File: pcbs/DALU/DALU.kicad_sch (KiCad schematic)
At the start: 1 part, among them J101 Conn_02x20_Odd_Even

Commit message: Last of the compute stages
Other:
- added sheet OR (OR.kicad_sch)
- sheet XOR ports: added A_{bus}, B_{bus}, XOR_{bus}; removed none
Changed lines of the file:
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@@
   (junction (at 46.99 68.58) (diameter 0) (color 0 0 0 0)
   )
+  (junction (at 82.55 46.99) (diameter 0) (color 0 0 0 0)
+  )
   (junction (at 78.74 29.21) (diameter 0) (color 0 0 0 0)
   )
   (junction (at 25.4 68.58) (diameter 0) (color 0 0 0 0)
   )
+  (junction (at 78.74 72.39) (diameter 0) (color 0 0 0 0)
+  )
+  (junction (at 78.74 52.07) (diameter 0) (color 0 0 0 0)
+  )
+  (junction (at 82.55 67.31) (diameter 0) (color 0 0 0 0)
+  )
   (bus_entry (at 60.96 50.8) (size -2.54 2.54)
     (stroke (width 0) (type default) (color 0 0 0 0))
@@
     (stroke (width 0) (type default) (color 0 0 0 0))
   )
+  (bus (pts (xy 78.74 52.07) (xy 78.74 72.39))
+    (stroke (width 0) (type default) (color 0 0 0 0))
+  )
   (bus (pts (xy 58.42 38.1) (xy 58.42 40.64))
     (stroke (width 0) (type default) (color 0 0 0 0))
@@
     (stroke (width 0) (type default) (color 0 0 0 0))
   )
+  (bus (pts (xy 78.74 72.39) (xy 87.63 72.39))
+    (stroke (width 0) (type default) (color 0 0 0 0))
+  )
   (wire (pts (xy 16.51 68.58) (xy 25.4 68.58))
     (stroke (width 0) (type default) (color 0 0 0 0))
@@
     (stroke (width 0) (type default) (color 0 0 0 0))
   )
+  (bus (pts (xy 78.74 72.39) (xy 78.74 91.44))
+    (stroke (width 0) (type default) (color 0 0 0 0))
+  )
+  (bus (pts (xy 82.55 67.31) (xy 87.63 67.31))
+    (stroke (width 0) (type default) (color 0 0 0 0))
+  )
+  (bus (pts (xy 82.55 46.99) (xy 82.55 67.31))
+    (stroke (width 0) (type default) (color 0 0 0 0))
+  )
   (wire (pts (xy 43.18 33.02) (xy 55.88 33.02))
     (stroke (width 0) (type default) (color 0 0 0 0))
@@
     (stroke (width 0) (type default) (color 0 0 0 0))
   )
+  (bus (pts (xy 82.55 67.31) (xy 82.55 87.63))
+    (stroke (width 0) (type default) (color 0 0 0 0))
+  )
   (wire (pts (xy 43.18 63.5) (xy 58.42 63.5))
     (stroke (width 0) (type default) (color 0 0 0 0))
@@
     (stroke (width 0) (type default) (color 0 0 0 0))
   )
+  (bus (pts (xy 78.74 91.44) (xy 87.63 91.44))
+    (stroke (width 0) (type default) (color 0 0 0 0))
+  )
   (bus (pts (xy 58.42 35.56) (xy 58.42 38.1))
     (stroke (width 0) (type default) (color 0 0 0 0))
@@
   )
   (wire (pts (xy 43.18 35.56) (xy 55.88 35.56))
+    (stroke (width 0) (type default) (color 0 0 0 0))
+  )
+  (bus (pts (xy 82.55 87.63) (xy 87.63 87.63))
     (stroke (width 0) (type default) (color 0 0 0 0))
   )
@@
       (effects (font (size 1.27 1.27)) (justify left top))
     )
+    (pin "A_{bus}" input (at 87.63 67.31 180)
+      (effects (font (size 1.27 1.27)) (justify left))
+    )
+    (pin "B_{bus}" input (at 87.63 72.39 180)
+      (effects (font (size 1.27 1.27)) (justify left))
+    )
+    (pin "XOR_{bus}" output (at 106.68 69.85 0)
+      (effects (font (size 1.27 1.27)) (justify right))
+    )
   )
   (sheet (at 87.63 22.86) (size 19.05 13.97) (fields_autoplaced)
@@
     )
   )
+  (sheet (at 87.63 83.82) (size 19.05 11.43) (fields_autoplaced)
+    (stroke (width 0.1524) (type solid) (color 0 0 0 0))
+    (fill (color 0 0 0 0.0000))
+    (property "Sheet name" "OR" (id 0) (at 87.63 83.1084 0)
+      (effects (font (size 1.27 1.27)) (justify left bottom))
+    )
+    (property "Sheet file" "OR.kicad_sch" (id 1) (at 87.63 95.8346 0)
+      (effects (font (size 1.27 1.27)) (justify left top))
+    )
+    (pin "A_{bus}" input (at 87.63 87.63 180)
+      (effects (font (size 1.27 1.27)) (justify left))
+    )
+    (pin "B_{bus}" input (at 87.63 91.44 180)
+      (effects (font (size 1.27 1.27)) (justify left))
+    )
+    (pin "OR_{bus}" output (at 106.68 88.9 0)
+      (effects (font (size 1.27 1.27)) (justify right))
+    )
+  )
   (sheet (at 87.63 43.18) (size 19.05 13.97) (fields_autoplaced)
     (stroke (width 0.1524) (type solid) (color 0 0 0 0))
@@
     (path "/c6ea6b53-9211-4c3c-9fbd-19ff7075ec1c" (page "3"))
     (path "/12f01842-90c1-4b07-bb63-297dee23d62f" (page "4"))
+    (path "/95c8ed90-5067-42ef-af82-1a4d464a971b" (page "5"))
   )
   (symbol_instances
@@
       (reference "#PWR0201") (unit 1) (value "GND") (footprint "")
     )
+    (path "/95c8ed90-5067-42ef-af82-1a4d464a971b/d2917962-5a4a-4a69-aaf2-f43483f15313"
+      (reference "#PWR?") (unit 1) (value "GND") (footprint "")
+    )
+    (path "/95c8ed90-5067-42ef-af82-1a4d464a971b/4a3697d2-7faa-484a-8bcb-b8e25fa6ff72"
+      (reference "D501") (unit 1) (value "1N4148") (footprint "Diode_THT:D_DO-35_SOD27_P7.62mm_Horizontal")
+    )
+    (path "/95c8ed90-5067-42ef-af82-1a4d464a971b/bb7d2965-ee1e-4dec-a199-3e00f2e0bc28"
+      (reference "D502") (unit 1) (value "1N4148") (footprint "Diode_THT:D_DO-35_SOD27_P7.62mm_Horizontal")
+    )
+    (path "/95c8ed90-5067-42ef-af82-1a4d464a971b/a1a7e2eb-7c7a-416d-b49a-5a4e31e405d0"
+      (reference "D503") (unit 1) (value "1N4148") (footprint "Diode_THT:D_DO-35_SOD27_P7.62mm_Horizontal")
+    )
+    (path "/95c8ed90-5067-42ef-af82-1a4d464a971b/e2dd1ad3-44c2-4bb1-b77e-ec4191e188b1"
+      (reference "D504") (unit 1) (value "1N4148") (footprint "Diode_THT:D_DO-35_SOD27_P7.62mm_Horizontal")
+    )
+    (path "/95c8ed90-5067-42ef-af82-1a4d464a971b/07a04b4b-943e-4706-905e-cecf4428214b"
+      (reference "D505") (unit 1) (value "1N4148") (footprint "Diode_THT:D_DO-35_SOD27_P7.62mm_Horizontal")
+    )
+    (path "/95c8ed90-5067-42ef-af82-1a4d464a971b/af0b345b-54e7-42a3-a286-538b1287836d"
+      (reference "D506") (unit 1) (value "1N4148") (footprint "Diode_THT:D_DO-35_SOD27_P7.62mm_Horizontal")
+    )
+    (path "/95c8ed90-5067-42ef-af82-1a4d464a971b/421d6b09-7fac-4770-86f8-5100d23c67b1"
+      (reference "D507") (unit 1) (value "1N4148") (footprint "Diode_THT:D_DO-35_SOD27_P7.62mm_Horizontal")
+    )
+    (path "/95c8ed90-5067-42ef-af82-1a4d464a971b/569a1e0a-7613-401f-98cd-f7d7ae658bd9"
+      (reference "D508") (unit 1) (value "1N4148") (footprint "Diode_THT:D_DO-35_SOD27_P7.62mm_Horizontal")
+    )
+    (path "/95c8ed90-5067-42ef-af82-1a4d464a971b/98e6afcd-7c0c-46fa-aa45-ceb39f9dcfaf"
+      (reference "D509") (unit 1) (value "1N4148") (footprint "Diode_THT:D_DO-35_SOD27_P7.62mm_Horizontal")
+    )
+    (path "/95c8ed90-5067-42ef-af82-1a4d464a971b/60bbdc9b-d936-4faf-9e28-6b40f0fd6cbf"
+      (reference "D510") (unit 1) (value "1N4148") (footprint "Diode_THT:D_DO-35_SOD27_P7.62mm_Horizontal")
+    )
+    (path "/95c8ed90-5067-42ef-af82-1a4d464a971b/fada2b91-ce17-4b8b-b1c7-d90cada8f840"
+      (reference "D511") (unit 1) (value "1N4148") (footprint "Diode_THT:D_DO-35_SOD27_P7.62mm_Horizontal")
+    )
+    (path "/95c8ed90-5067-42ef-af82-1a4d464a971b/1894f8d6-098f-4396-911d-8aaa729e1f4d"
+      (reference "D512") (unit 1) (value "1N4148") (footprint "Diode_THT:D_DO-35_SOD27_P7.62mm_Horizontal")
+    )
+    (path "/95c8ed90-5067-42ef-af82-1a4d464a971b/29edd219-0759-4f76-a9cf-bbf5f6d146f1"
+      (reference "D513") (unit 1) (value "1N4148") (footprint "Diode_THT:D_DO-35_SOD27_P7.62mm_Horizontal")
+    )
+    (path "/95c8ed90-5067-42ef-af82-1a4d464a971b/05c0b09a-3745-46e5-8419-974dbbc659de"
+      (reference "D514") (unit 1) (value "1N4148") (footprint "Diode_THT:D_DO-35_SOD27_P7.62mm_Horizontal")
+    )
+    (path "/95c8ed90-5067-42ef-af82-1a4d464a971b/958ba730-cb10-4605-bd9f-9622ef54c965"
+      (reference "D515") (unit 1) (value "1N4148") (footprint "Diode_THT:D_DO-35_SOD27_P7.62mm_Horizontal")
+    )
+    (path "/95c8ed90-5067-42ef-af82-1a4d464a971b/2b0a17ac-d926-4d0e-b18e-f9a3a2894ef9"
+      (reference "D516") (unit 1) (value "1N4148") (footprint "Diode_THT:D_DO-35_SOD27_P7.62mm_Horizontal")
+    )
     (path "/0078be7f-ebde-4855-a007-c3409b021a3e"
       (reference "J101") (unit 1) (value "Conn_02x20_Odd_Even") (footprint "Connector_PinHeader_2.54mm:PinHeader_2x20_P2.54mm_Vertical")
     )
+    (path "/95c8ed90-5067-42ef-af82-1a4d464a971b/9b8f5155-1304-4993-8373-bc373de0a39a"
+      (reference "R501") (unit 1) (value "100k") (footprint "Resistor_THT:R_Axial_DIN0207_L6.3mm_D2.5mm_P7.62mm_Horizontal")
+    )
+    (path "/95c8ed90-5067-42ef-af82-1a4d464a971b/158d25e5-8ec9-4037-a0c2-61fe1e6ce44b"
+      (reference "R502") (unit 1) (value "100k") (footprint "Resistor_THT:R_Axial_DIN0207_L6.3mm_D2.5mm_P7.62mm_Horizontal")
+    )
+    (path "/95c8ed90-5067-42ef-af82-1a4d464a971b/f4092d13-ae6a-4ea0-837d-8731ed399cc1"
+      (reference "R503") (unit 1) (value "100k") (footprint "Resistor_THT:R_Axial_DIN0207_L6.3mm_D2.5mm_P7.62mm_Horizontal")
+    )
+    (path "/95c8ed90-5067-42ef-af82-1a4d464a971b/872041c3-3b2a-4e80-9cc8-3a2c263148c4"
+      (reference "R504") (unit 1) (value "100k") (footprint "Resistor_THT:R_Axial_DIN0207_L6.3mm_D2.5mm_P7.62mm_Horizontal")
+    )
+    (path "/95c8ed90-5067-42ef-af82-1a4d464a971b/d5f1b087-ebb8-409e-b54e-e6f86f6d7838"
+      (reference "R505") (unit 1) (value "100k") (footprint "Resistor_THT:R_Axial_DIN0207_L6.3mm_D2.5mm_P7.62mm_Horizontal")
+    )
+    (path "/95c8ed90-5067-42ef-af82-1a4d464a971b/aeb0dafe-31b3-4371-a164-439c8eb5842e"
+      (reference "R506") (unit 1) (value "100k") (footprint "Resistor_THT:R_Axial_DIN0207_L6.3mm_D2.5mm_P7.62mm_Horizontal")
+    )
+    (path "/95c8ed90-5067-42ef-af82-1a4d464a971b/563e37ab-bd17-438f-98ec-d1d2cc39a8d4"
+      (reference "R507") (unit 1) (value "100k") (footprint "Resistor_THT:R_Axial_DIN0207_L6.3mm_D2.5mm_P7.62mm_Horizontal")
+    )
+    (path "/95c8ed90-5067-42ef-af82-1a4d464a971b/95fb95c2-98e6-41b7-ac87-417ac8aebac9"
+      (reference "R508") (unit 1) (value "100k") (footprint "Resistor_THT:R_Axial_DIN0207_L6.3mm_D2.5mm_P7.62mm_Horizontal")
+    )
     (path "/70795f93-2efa-413c-baa8-a557a86ea734/e43fe007-808a-4034-8733-705344372de1"

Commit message: Trying to figure out the hierarchical buses
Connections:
- net C0: now reaches J101.3 (Pin_3)
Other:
- added sheet Output Stage (output.kicad_sch)
- sheet AND-NAND ports: added A[0..7], B[0..7], NAND[0..7]; removed AND/NAND_{bus}, A_{bus}, B_{bus}
- sheet Adder-Subtractor ports: added AS[0..7], A[0..7], B[0..7]; removed ADD/SUB_{bus}, A_{bus}, B_{bus}
- sheet OR ports: added A[0..7], B[0..7], OR[0..7]; removed A_{bus}, B_{bus}, OR_{bus}
- sheet XOR ports: added A[0..7], B[0..7], XOR[0..7]; removed A_{bus}, B_{bus}, XOR_{bus}

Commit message: Trying to get everything together
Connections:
- net A0: no longer names the net of J101.18 (Pin_18)
- net A1: no longer names the net of J101.16 (Pin_16)
- net A2: no longer names the net of J101.14 (Pin_14)
- net A3: no longer names the net of J101.12 (Pin_12)
- net A4: no longer names the net of J101.10 (Pin_10)
- net A5: no longer names the net of J101.8 (Pin_8)
- net A6: no longer names the net of J101.6 (Pin_6)
- net A7 renamed A.A7
- net C0 renamed C_{bus}0
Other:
- sheet Adder-Subtractor renamed AdderSubtractor
- sheet Output Stage ports: added ADDSUB[0..7], C_{bus}[0..7]; removed AS[0..7], C_{bus}

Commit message: Thinking about some of the control logic
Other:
- sheet Output Stage ports: added none; removed C_{bus}[0..7]

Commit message: Thinking about SMD assembly. Will be rethinking
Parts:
- added U101, U102: 74HC245, Package_SO:SOIC-20W_7.5x12.8mm_P1.27mm, symbol 74xx:74HC245
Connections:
- net at J101.10 (Pin_10): now also U101.5 (A3)
- net at J101.12 (Pin_12): now also U101.6 (A4)
- net at J101.14 (Pin_14): now also U101.7 (A5)
- net at J101.16 (Pin_16): now also U101.8 (A6)
- net at J101.18 (Pin_18): now also U101.9 (A7)
- net at J101.6 (Pin_6): now also U101.3 (A1)
- net at J101.8 (Pin_8): now also U101.4 (A2)
- net A.A7: no longer names the net of J101.4 (Pin_4)
- net A.A7: now also U101.2 (A0)
- net B0: no longer names the net of J101.38 (Pin_38)
- net B0: now also U102.9 (A7)
- net B1: no longer names the net of J101.36 (Pin_36)
- net B1: now also U102.8 (A6)
- net B2: no longer names the net of J101.34 (Pin_34)
- net B2: now also U102.7 (A5)
- net B3: no longer names the net of J101.32 (Pin_32)
- net B3: now also U102.6 (A4)
- net B4: no longer names the net of J101.30 (Pin_30)
- net B4: now also U102.5 (A3)
- net B5: no longer names the net of J101.28 (Pin_28)
- net B5: now also U102.4 (A2)
- net B6: no longer names the net of J101.26 (Pin_26)
- net B6: now also U102.3 (A1)
- net B7: no longer names the net of J101.24 (Pin_24)
- net B7: now also U102.2 (A0)
- net C_{bus}0: no longer names the net of J101.3 (Pin_3)
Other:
- moved on the sheet: J101

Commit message: Doing some rethinking
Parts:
- removed J101: Conn_02x20_Odd_Even, Connector_PinHeader_2.54mm:PinHeader_2x20_P2.54mm_Vertical, symbol Connector_Generic:Conn_02x20_Odd_Even
- removed U101, U102: 74HC245, Package_SO:SOIC-20W_7.5x12.8mm_P1.27mm, symbol 74xx:74HC245
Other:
- added sheet Connector (connector.kicad_sch)

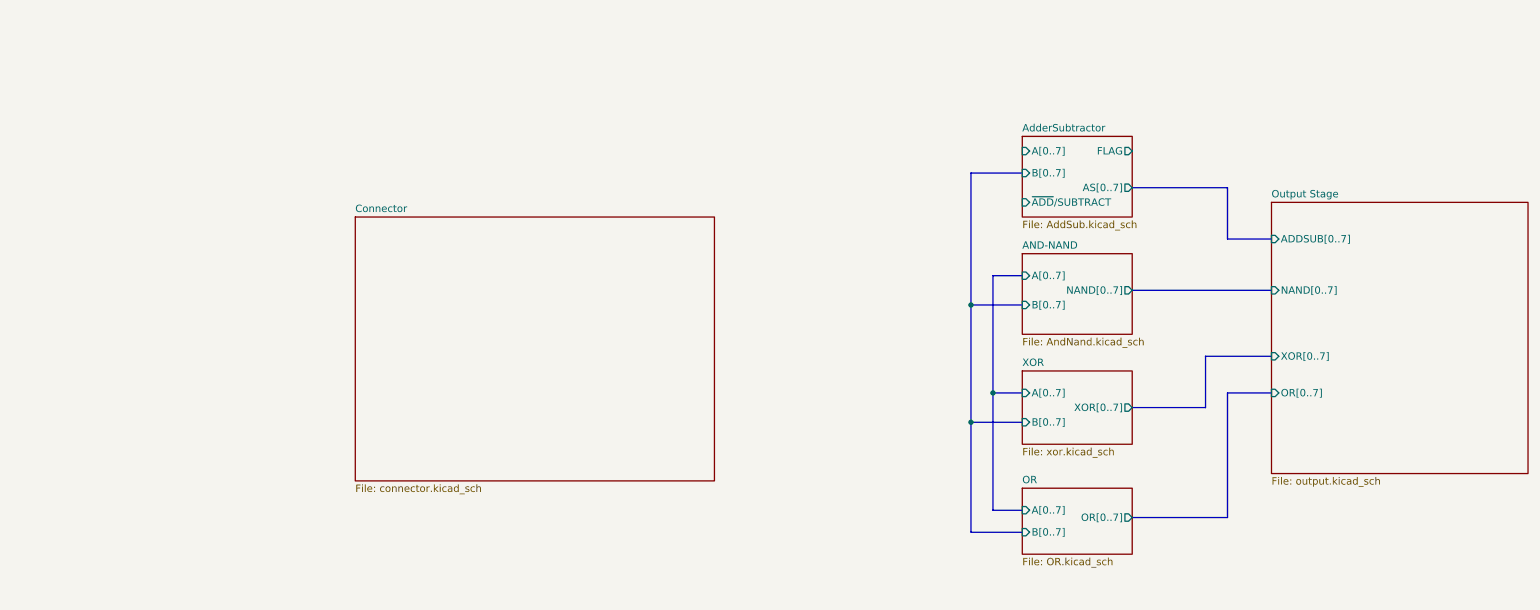
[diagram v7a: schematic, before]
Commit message: Input stage fiddling
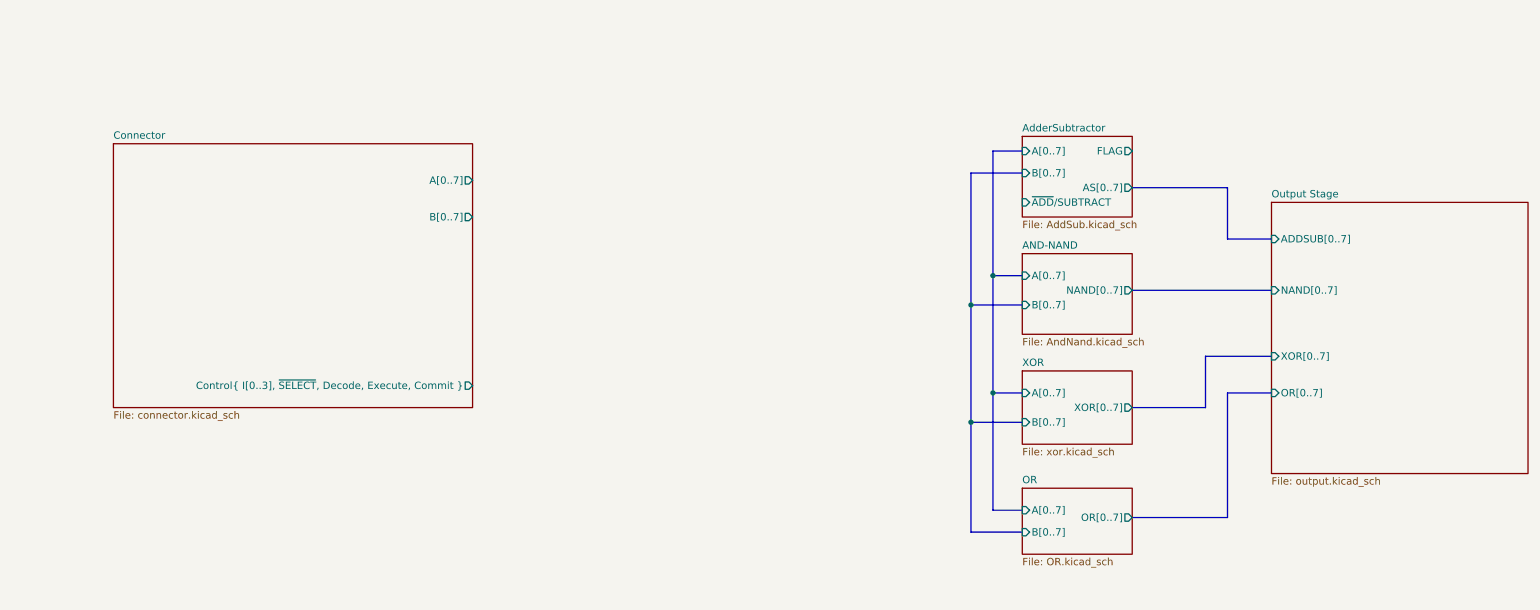
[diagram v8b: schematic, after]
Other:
- sheet Connector ports: added A[0..7], B[0..7], Control{ I[0..3], ~{SELECT}, Decode, Execute, Commit }; removed none
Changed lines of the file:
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@@
   (junction (at 180.34 82.55) (diameter 0) (color 0 0 0 0)
   )
+  (junction (at 184.15 57.15) (diameter 0) (color 0 0 0 0)
+  )
   (junction (at 180.34 62.23) (diameter 0) (color 0 0 0 0)
   )
@@
     (stroke (width 0) (type default) (color 0 0 0 0))
   )
+  (bus (pts (xy 184.15 35.56) (xy 189.23 35.56))
+    (stroke (width 0) (type default) (color 0 0 0 0))
+  )
   (bus (pts (xy 224.79 77.47) (xy 232.41 77.47))
     (stroke (width 0) (type default) (color 0 0 0 0))
@@
   )
   (bus (pts (xy 184.15 57.15) (xy 189.23 57.15))
+    (stroke (width 0) (type default) (color 0 0 0 0))
+  )
+  (bus (pts (xy 184.15 57.15) (xy 184.15 35.56))
     (stroke (width 0) (type default) (color 0 0 0 0))
   )
@@
     )
   )
-  (sheet (at 73.66 46.99) (size 62.23 45.72) (fields_autoplaced)
+  (sheet (at 31.75 34.29) (size 62.23 45.72) (fields_autoplaced)
     (stroke (width 0.1524) (type solid) (color 0 0 0 0))
     (fill (color 0 0 0 0.0000))
-    (property "Sheet name" "Connector" (id 0) (at 73.66 46.2784 0)
+    (property "Sheet name" "Connector" (id 0) (at 31.75 33.5784 0)
       (effects (font (size 1.27 1.27)) (justify left bottom))
     )
-    (property "Sheet file" "connector.kicad_sch" (id 1) (at 73.66 93.2946 0)
+    (property "Sheet file" "connector.kicad_sch" (id 1) (at 31.75 80.5946 0)
       (effects (font (size 1.27 1.27)) (justify left top))
+    )
+    (pin "A[0..7]" output (at 93.98 40.64 0)
+      (effects (font (size 1.27 1.27)) (justify right))
+    )
+    (pin "Control{ I[0..3], ~{SELECT}, Decode, Execute, Commit }" output (at 93.98 76.2 0)
+      (effects (font (size 1.27 1.27)) (justify right))
+    )
+    (pin "B[0..7]" output (at 93.98 46.99 0)
+      (effects (font (size 1.27 1.27)) (justify right))
     )
   )
@@
       (reference "#PWR0718") (unit 1) (value "GND") (footprint "")
     )
+    (path "/5a7cb513-9739-4d2d-a582-8607360c12f9/21d95115-dbd9-470e-8e19-1960bb6f6324"
+      (reference "#PWR?") (unit 1) (value "GND") (footprint "")
+    )
+    (path "/5a7cb513-9739-4d2d-a582-8607360c12f9/80b492a5-fd4d-44b4-9dea-06998740736c"
+      (reference "#PWR?") (unit 1) (value "GND") (footprint "")
+    )
+    (path "/5a7cb513-9739-4d2d-a582-8607360c12f9/d1aa965e-169e-4b67-aca0-50fad862f64e"
+      (reference "#PWR?") (unit 1) (value "GND") (footprint "")
+    )
     (path "/95c8ed90-5067-42ef-af82-1a4d464a971b/4a3697d2-7faa-484a-8bcb-b8e25fa6ff72"
       (reference "D601") (unit 1) (value "1N4148") (footprint "Diode_THT:D_DO-35_SOD27_P7.62mm_Horizontal")
@@
       (reference "U402") (unit 5) (value "74HC00") (footprint "Package_DIP:DIP-14_W7.62mm_Socket")
     )
+    (path "/c6ea6b53-9211-4c3c-9fbd-19ff7075ec1c/0ec7035b-ccb5-43bc-b8f5-bca38c208175"
+      (reference "U403") (unit 1) (value "74HC14") (footprint "Package_SO:SOIC-14_3.9x8.7mm_P1.27mm")
+    )
+    (path "/c6ea6b53-9211-4c3c-9fbd-19ff7075ec1c/292da1ac-5d5b-4b90-a98b-0a23ed154e2a"
+      (reference "U403") (unit 2) (value "74HC14") (footprint "Package_SO:SOIC-14_3.9x8.7mm_P1.27mm")
+    )
+    (path "/c6ea6b53-9211-4c3c-9fbd-19ff7075ec1c/9474edcf-0a86-480e-a097-6025e2d77e58"
+      (reference "U403") (unit 3) (value "74HC14") (footprint "Package_SO:SOIC-14_3.9x8.7mm_P1.27mm")
+    )
+    (path "/c6ea6b53-9211-4c3c-9fbd-19ff7075ec1c/b7cf4de2-e018-4c3e-8ca5-4623af79397a"
+      (reference "U403") (unit 4) (value "74HC14") (footprint "Package_SO:SOIC-14_3.9x8.7mm_P1.27mm")
+    )
+    (path "/c6ea6b53-9211-4c3c-9fbd-19ff7075ec1c/9c79a204-b128-431d-8332-383be6aa4922"
+      (reference "U403") (unit 5) (value "74HC14") (footprint "Package_SO:SOIC-14_3.9x8.7mm_P1.27mm")
+    )
+    (path "/c6ea6b53-9211-4c3c-9fbd-19ff7075ec1c/e789c5a2-2565-4eea-a7fe-35b1715f7e95"
+      (reference "U403") (unit 6) (value "74HC14") (footprint "Package_SO:SOIC-14_3.9x8.7mm_P1.27mm")
+    )
+    (path "/c6ea6b53-9211-4c3c-9fbd-19ff7075ec1c/d4b9fecf-a2fa-4b48-aeec-2d56d7bae2fb"
+      (reference "U403") (unit 7) (value "74HC14") (footprint "Package_SO:SOIC-14_3.9x8.7mm_P1.27mm")
+    )
+    (path "/c6ea6b53-9211-4c3c-9fbd-19ff7075ec1c/8eae6d7f-a3b0-4d57-b6c8-9a88e6d04fac"
+      (reference "U404") (unit 1) (value "74HC14") (footprint "Package_SO:SOIC-14_3.9x8.7mm_P1.27mm")
+    )
+    (path "/c6ea6b53-9211-4c3c-9fbd-19ff7075ec1c/636ad6bd-3a0c-45de-929c-17741e44e3c9"
+      (reference "U404") (unit 2) (value "74HC14") (footprint "Package_SO:SOIC-14_3.9x8.7mm_P1.27mm")
+    )
+    (path "/c6ea6b53-9211-4c3c-9fbd-19ff7075ec1c/4dda6550-53ed-4e78-9b74-0c669af7c820"
+      (reference "U404") (unit 3) (value "74HC14") (footprint "Package_SO:SOIC-14_3.9x8.7mm_P1.27mm")
+    )
+    (path "/c6ea6b53-9211-4c3c-9fbd-19ff7075ec1c/c6a9419d-eea5-4e67-957d-0cdaa4736f24"
+      (reference "U404") (unit 4) (value "74HC14") (footprint "Package_SO:SOIC-14_3.9x8.7mm_P1.27mm")
+    )
+    (path "/c6ea6b53-9211-4c3c-9fbd-19ff7075ec1c/2046ff3a-bc6b-41d6-ab4d-10407d9a9598"
+      (reference "U404") (unit 5) (value "74HC14") (footprint "Package_SO:SOIC-14_3.9x8.7mm_P1.27mm")
+    )
+    (path "/c6ea6b53-9211-4c3c-9fbd-19ff7075ec1c/d8f16c03-3c09-439d-acba-5845e19c92c8"
+      (reference "U404") (unit 6) (value "74HC14") (footprint "Package_SO:SOIC-14_3.9x8.7mm_P1.27mm")
+    )
+    (path "/c6ea6b53-9211-4c3c-9fbd-19ff7075ec1c/23aa2f06-10df-4a14-881b-5fa48c60928e"
+      (reference "U404") (unit 7) (value "74HC14") (footprint "Package_SO:SOIC-14_3.9x8.7mm_P1.27mm")
+    )
     (path "/c6ea6b53-9211-4c3c-9fbd-19ff7075ec1c/d09eae53-7b44-4f21-b5f2-7194aa32bf43"
-      (reference "U403") (unit 1) (value "74HC245") (footprint "Package_SO:SOIC-20W_7.5x12.8mm_P1.27mm")
+      (reference "U405") (unit 1) (value "74HC245") (footprint "Package_SO:SOIC-20W_7.5x12.8mm_P1.27mm")
     )
     (path "/c6ea6b53-9211-4c3c-9fbd-19ff7075ec1c/dcb7de3f-7c04-4bfb-93fe-259db1e9adf0"
-      (reference "U404") (unit 1) (value "74HC245") (footprint "Package_SO:SOIC-20W_7.5x12.8mm_P1.27mm")
+      (reference "U406") (unit 1) (value "74HC245") (footprint "Package_SO:SOIC-20W_7.5x12.8mm_P1.27mm")
     )
     (path "/12f01842-90c1-4b07-bb63-297dee23d62f/23fac53d-9ffc-48cb-b276-ba599141a573"
